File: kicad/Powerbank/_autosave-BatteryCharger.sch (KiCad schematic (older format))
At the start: 48 parts, among them IC4 BQ25703ARSNT, Q4 Q_NMOS_GDS, Q5 Q_NMOS_GDS, Q8 Q_PMOS_GDS

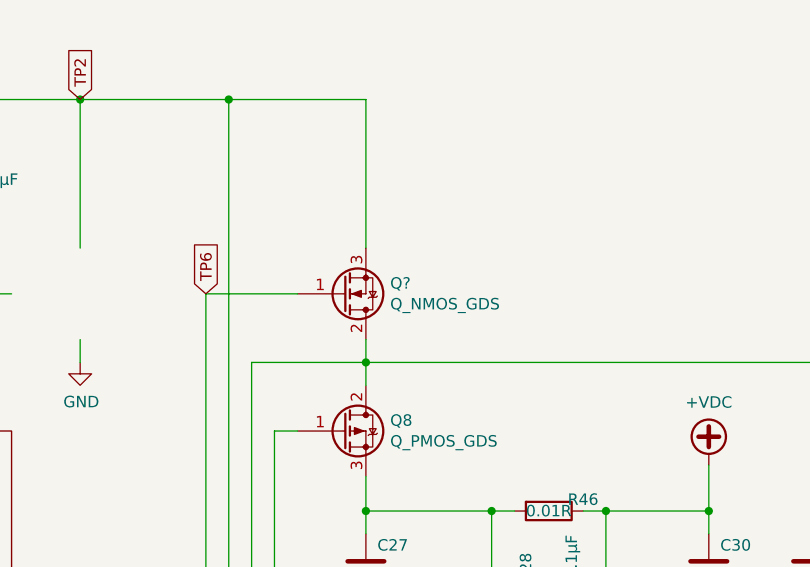
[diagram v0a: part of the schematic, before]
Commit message: Added footprint for all, moved to a first attempt for routing
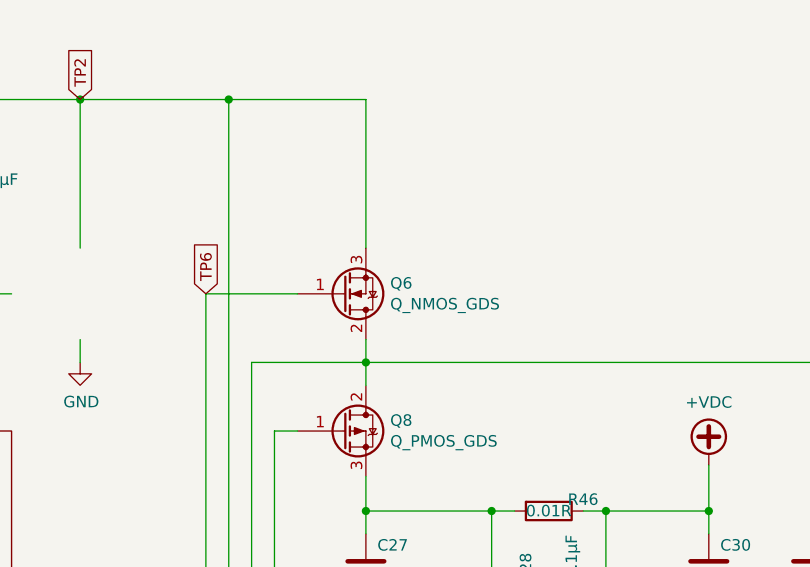
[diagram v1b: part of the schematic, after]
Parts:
- gave numbers to parts that had none: 1
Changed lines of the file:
@@
 $EndComp
 $Comp
-L Device:Q_NMOS_GDS Q?
+L Device:Q_NMOS_GDS Q6
 U 1 1 5E20690D
 P 7850 2450
-F 0 "Q?" H 8056 2404 50  0000 L CNN
+F 0 "Q6" H 8056 2404 50  0000 L CNN
 F 1 "Q_NMOS_GDS" H 8056 2495 50  0000 L CNN
 F 2 "Package_TO_SOT_SMD:TO-252-3_TabPin2" H 8050 2550 50  0001 C CNN
